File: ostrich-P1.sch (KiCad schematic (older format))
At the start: 1 part

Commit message: 1 motor driver done
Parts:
- added 10K: R, symbol R
- added J?: E, symbol Conn_01x04
- added J?: EXP1, symbol Conn_02x05_Counter_Clockwise
- added J?: EXP2, symbol Conn_02x05_Counter_Clockwise
- added U?: SilentStepStick, symbol SilentStepStick
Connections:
- net MISO: now reaches SHIELD?.50 (PB3_(MISO))
- net MISO: now also U?.13 (SDO)
- net MOSI: now reaches SHIELD?.51 (PB2_(MOSI))
- net MOSI: now also U?.10 (SDI)
- net SCK: now reaches SHIELD?.52 (PB1_(SCK))
- net SCK: now also U?.11 (SCK)
- new net: 10K.2, J?.1 (Pin_1)
- new net CS_Eax: U?.12 (CS)
- new net D16: J?.4 (Pin_4)
- new net D17: J?.7 (Pin_7)
- new net D23: J?.8 (Pin_8)
- new net D25: J?.3 (Pin_3)
- new net D27: J?.9 (Pin_9)
- new net D29: J?.2 (Pin_2)
- new net D31: J?.7 (Pin_7)
- new net D33: J?.8 (Pin_8)
- new net D35: J?.5 (Pin_5)
- new net D37: J?.6 (Pin_6)
- new net D41: J?.2 (Pin_2)
- new net D49: J?.9 (Pin_9)
- new net D50: J?.6 (Pin_6)
- new net D51: J?.3 (Pin_3)
- new net D52: J?.5 (Pin_5)
- new net D53: J?.4 (Pin_4)
- new net DIAG1_Eax: U?.17 (DIAG1)
- new net DIR_Eax: U?.16 (DIR)
- new net EN_Eax: U?.9 (En)
- new net GND: J?.10 (Pin_10), J?.10 (Pin_10), U?.1 (GND), U?.7 (GND)
- new net M1A_Eax: J?.3 (Pin_3), U?.4 (M1A)
- new net M1B_Eax: J?.4 (Pin_4), U?.3 (M1B)
- new net M2A_Eax: J?.2 (Pin_2), U?.5 (M2A)
- new net M2B_Eax: J?.1 (Pin_1), U?.6 (M2B)
- new net STEP_Eax: U?.15 (STEP)
- new net VCC: 10K.1, J?.1 (Pin_1), U?.2 (VIO)
- new net VDC: U?.8 (VM)
- no-connect marks 0 -> 3
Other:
- note added: "Don't know about this pin"

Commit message: Brownout detector done
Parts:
- added 330R, 3M3 (x2), 510K, 910K: R, symbol R
- added C?: 47uF, symbol CP
- added D?: 1N4148, symbol D
- added D?: Q_TRIAC_AAG, symbol Q_TRIAC_AAG
- added J?: bedsens, symbol Conn_01x03
- added J?: Earth, symbol Conn_01x01
- added J?: Neutral, symbol Conn_01x01
- added J?: Bed, symbol Conn_01x01
- added U? (x2): LM393, symbol LM393
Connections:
- net GND: now also 3M3.2, 3M3.2, C?.2, U?.4 (V-)
- net VDC: now also 330R.1, 510K.1, U?.8 (V+)
- new net: 910K.1, C?.1, D?.1 (K)
- new net: 330R.2, D?.2 (A)
- new net: 3M3.1, 910K.2, U?.2 (_)
- new net: 3M3.1, 510K.2, U?.3 (+)
- new net BRWN: U?.1
- new net Earth_Protective: J?.1 (Pin_1)
- new net NEUT: J?.1 (Pin_1)
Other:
- note added: "Brownout detector"
- note added: "HOTBED"

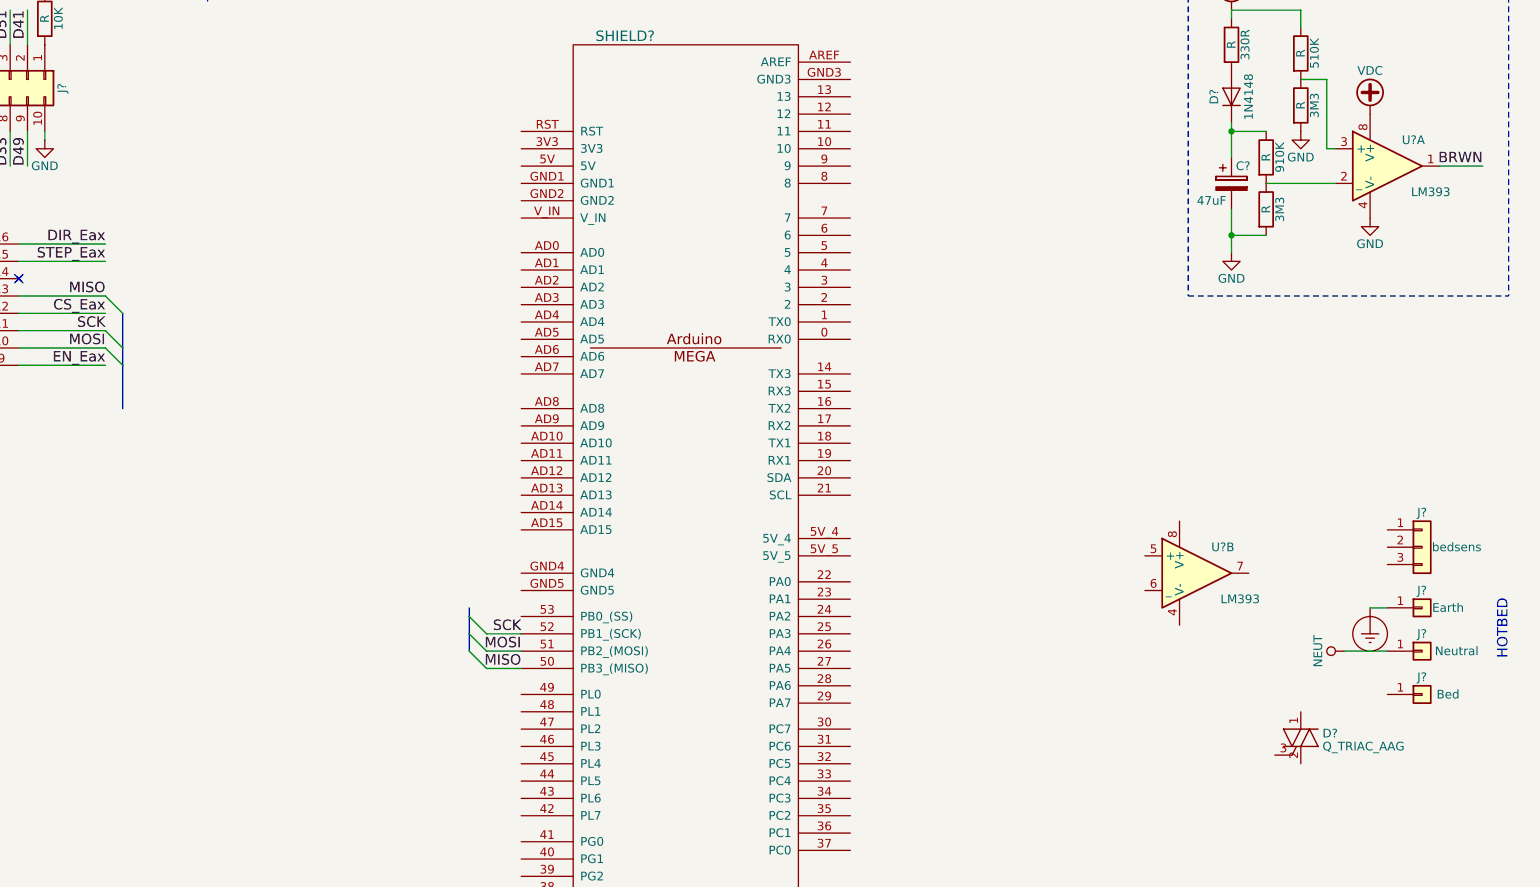
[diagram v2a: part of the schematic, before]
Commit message: HOTBED SSR done
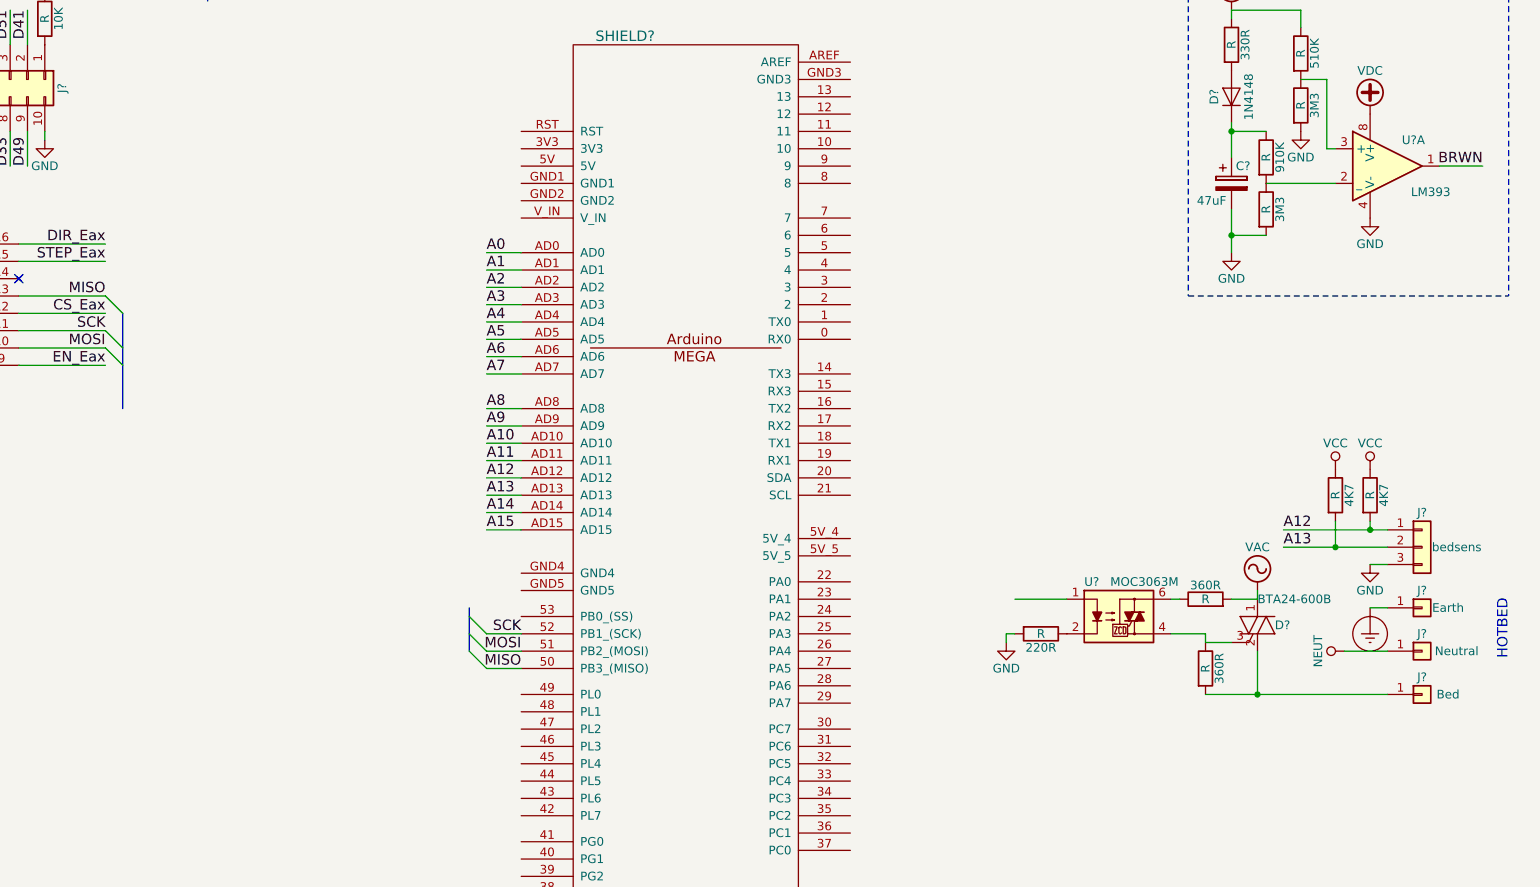
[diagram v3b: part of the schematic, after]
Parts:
- removed U?: LM393, symbol LM393
- added 220R, 360R (x2), 4K7 (x2): R, symbol R
- added U?: MOC3063M, symbol MOC3063M
- D?: value Q_TRIAC_AAG -> BTA24-600B
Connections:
- net GND: now also J?.3 (Pin_3), 220R.2
- net VCC: now also 4K7.1, 4K7.1
- net A0: now reaches SHIELD?.AD0
- net A1: now reaches SHIELD?.AD1
- net A10: now reaches SHIELD?.AD10
- net A11: now reaches SHIELD?.AD11
- net A12: now reaches SHIELD?.AD12
- net A12: now also J?.1 (Pin_1), 4K7.2
- net A13: now reaches SHIELD?.AD13
- net A13: now also J?.2 (Pin_2), 4K7.2
- net A14: now reaches SHIELD?.AD14
- net A15: now reaches SHIELD?.AD15
- net A2: now reaches SHIELD?.AD2
- net A3: now reaches SHIELD?.AD3
- net A4: now reaches SHIELD?.AD4
- net A5: now reaches SHIELD?.AD5
- net A6: now reaches SHIELD?.AD6
- net A7: now reaches SHIELD?.AD7
- net A8: now reaches SHIELD?.AD8
- net A9: now reaches SHIELD?.AD9
- net at J?.1 (Pin_1): now also D?.2 (A2), 360R.2
- net VAC: now reaches D?.1 (A1)
- net VAC: now also 360R.2
- net at D?.3 (G): now also 360R.1, U?.4
- new net: 220R.1, U?.2
- new net: 360R.1, U?.6
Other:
- moved on the sheet: D?

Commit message: 3.3V reg and ESP12
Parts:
- added 1R, 220R?, 330R? (x2), 4K? (x2), R? (x2): R, symbol R
- added C?: 10uF, symbol C
- added D? (x2): LED, symbol LED
- added D?: BTA24-600B, symbol Q_TRIAC_AAG
- added J?: bedsens, symbol Conn_01x03
- added J?: Earth, symbol Conn_01x01
- added J?: Neutral, symbol Conn_01x01
- added J?: End, symbol Conn_01x01
- added U?: MOC3063M, symbol MOC3063M
- added U?: LM1117-3.3, symbol LM1117-3.3
- added U?: ESP-12F, symbol ESP-12F
- renumbered 360R to 330R
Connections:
- net A12: now also 4K?.2, J?.1 (Pin_1)
- net A13: now also 4K?.2, J?.2 (Pin_2)
- net Earth_Protective: now also J?.1 (Pin_1)
- net GND: now also 220R.1, 220R?.1, C?.2, J?.3 (Pin_3), R?.1, R?.1, U?.1 (GND), U?.9 (GND); no longer 220R.2
- net NEUT: now also J?.1 (Pin_1)
- net VAC: now also 330R?.2, D?.1 (A1)
- net VCC: now also 4K?.1, 4K?.1, U?.3 (VI)
- net BedC: now reaches U?.1
- net at U?.2: now also 220R.2; no longer 220R.1
- new net: D?.1 (K), R?.2 (x2)
- new net: 330R?.2, D?.2 (A2), J?.1 (Pin_1)
- new net: 330R?.1, D?.3 (G), U?.4
- new net: 220R?.2, U?.2
- new net: 330R?.1, U?.6
- new net: 1R.2, C?.1
- new net +3V3: 1R.1, U?.2 (VO), U?.8 (VCC)
- new net EndC: U?.1
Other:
- note added: "BED"
- note added: "END"
- note removed: "HOTBED"
- moved on the sheet: 220R, 330R, 4K7, D?, J?, U?

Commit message: Added buck converter
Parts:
- added U?: Buck-Converter, symbol Buck-Converter
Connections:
- net GND: now also U?.3 (OUT-), U?.4 (OUT-), U?.5 (IN-), U?.6 (IN-)
- net VCC: now also U?.1 (OUT+), U?.2 (OUT+)
- net VDC: now also U?.7 (IN+), U?.8 (IN+)
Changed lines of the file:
@@
 Wire Wire Line
 	7400 7900 7350 7900
+$Comp
+L Buck-Converter U?
+U 1 1 5AFC21BD
+P 6400 0
+F 0 "U?" H 6400 -100 60  0000 C CNN
+F 1 "Buck-Converter" H 6400 0   60  0000 C CNN
+F 2 "" H 6400 0   60  0001 C CNN
+F 3 "" H 6400 0   60  0001 C CNN
+	1    6400 0
+	1    0    0    -1
+$EndComp
+$Comp
+L VDC #PWR?
+U 1 1 5AFC32E0
+P 6950 -200
+F 0 "#PWR?" H 6950 -300 50  0001 C CNN
+F 1 "VDC" H 6950 50  50  0000 C CNN
+F 2 "" H 6950 -200 50  0001 C CNN
+F 3 "" H 6950 -200 50  0001 C CNN
+	1    6950 -200
+	1    0    0    -1
+$EndComp
+$Comp
+L VCC #PWR?
+U 1 1 5AFC334E
+P 5850 -200
+F 0 "#PWR?" H 5850 -350 50  0001 C CNN
+F 1 "VCC" H 5850 -50 50  0000 C CNN
+F 2 "" H 5850 -200 50  0001 C CNN
+F 3 "" H 5850 -200 50  0001 C CNN
+	1    5850 -200
+	1    0    0    -1
+$EndComp
+$Comp
+L GND #PWR?
+U 1 1 5AFC33BC
+P 5850 250
+F 0 "#PWR?" H 5850 0   50  0001 C CNN
+F 1 "GND" H 5850 100 50  0000 C CNN
+F 2 "" H 5850 250 50  0001 C CNN
+F 3 "" H 5850 250 50  0001 C CNN
+	1    5850 250
+	1    0    0    -1
+$EndComp
+$Comp
+L GND #PWR?
+U 1 1 5AFC342A
+P 6950 250
+F 0 "#PWR?" H 6950 0   50  0001 C CNN
+F 1 "GND" H 6950 100 50  0000 C CNN
+F 2 "" H 6950 250 50  0001 C CNN
+F 3 "" H 6950 250 50  0001 C CNN
+	1    6950 250
+	1    0    0    -1
+$EndComp
+Wire Wire Line
+	6950 250  6950 150
+Wire Wire Line
+	6950 -100 6950 -200
+Wire Wire Line
+	5850 -200 5850 -100
+Wire Wire Line
+	5850 150  5850 250
 $EndSCHEMATC

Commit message: added a couple of mosfets
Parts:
- added 1K: R, symbol R
- added D? (x3): LED, symbol LED
- added J?: Stepfan, symbol Conn_01x02
- added J?: Compressor, symbol Conn_01x02
- added J?: Chamber fan, symbol Conn_01x02
- added Q?: S8050, TO_SOT_Packages_THT:TO-92_Molded_Narrow, symbol S8050
- added Q?: IRF3708, symbol Q_NMOS_DGS
- added Q?: IRLZ44N, symbol Q_NMOS_DGS
- added R? (x3): 1K, symbol R
- J?: value bedsens -> chasens
- R?: renamed from 10K; value R -> 10K
- R?: renamed from 910K; value R -> 910K
- R? (x2): renamed from 3M3; value R -> 3M3
- R?: renamed from 510K; value R -> 510K
- R? (x3): renamed from 330R; value R -> 330R
- R? (x2): renamed from 4K7; value R -> 4K7
- R?: renamed from 220R; value R -> 220R
- R? (x2): value R -> 1K
- R? (x2): renamed from 4K?; value R -> 4K7
- R?: renamed from 220R?; value R -> 220R
- R? (x2): renamed from 330R?; value R -> 330R
- R?: renamed from 1R; value R -> 1R
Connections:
- net GND: now also Q?.1 (E), Q?.3 (S), Q?.3 (S), R?.2, R?.2, R?.2
- net VDC: now also J?.1 (Pin_1), J?.1 (Pin_1), J?.1 (Pin_1)
- new net: J?.2 (Pin_2), Q?.3 (C)
- new net: 1K.1, Q?.2 (B)
- new net: D?.1 (K), R?.1 (x3)
- new net: J?.2 (Pin_2), Q?.1 (D) (x2)
- new net ChafanC: D?.2 (A), Q?.2 (G)
- new net CompC: D?.2 (A), Q?.2 (G)
- new net StepfanC: 1K.2, D?.2 (A)
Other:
- note added: "CHAMBER"
- note removed: "END"
